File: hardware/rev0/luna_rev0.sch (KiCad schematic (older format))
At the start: 34 parts, among them J1 USB_B_Micro, J2 USB_B_Micro, J3 USB_A, J4 USB_B_Micro, J7 Conn_02x02_Counter_Clockwise, J8 Conn_Coaxial, J9 Conn_Coaxial, SW1 BTN_RECOVERY, SW2 BTN_DFU, SW3 BTN_RESET, U1 AP22814-SOT, U12 AP22814-SOT, Y1 DSC60xx

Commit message: hardware: add part numbers
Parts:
- C53: Description (none) -> CAP CER 10UF 10V X5R 0805; Manufacturer_Name (none) -> Taiyo Yuden; Manufacturer_Part_Number (none) -> LMK212ABJ106KGHT
- D1, D8: Description (none) -> DIODE SCHOTTKY 30V 5A SOD128; Manufacturer_Name (none) -> Nexperia; Manufacturer_Part_Number (none) -> PMEG3050EP,115
- D2: Manufacturer_Part_Number (none) -> GENERIC-LED-0603-RED
- D3: Manufacturer_Part_Number (none) -> GENERIC-LED-0603-ORANGE
- D4: Manufacturer_Part_Number (none) -> GENERIC-LED-0603-YELLOW
- D5: Manufacturer_Part_Number (none) -> GENERIC-LED-0603-GREEN
- D6: Manufacturer_Part_Number (none) -> GENERIC-LED-0603-BLUE
- D7: Manufacturer_Part_Number (none) -> GENERIC-LED-0603-PURPLE
- J1, J2, J4: Description (none) -> CONN RCPT USB2.0 MICRO B SMD R/A; Manufacturer_Name (none) -> Amphenol ICC; Manufacturer_Part_Number (none) -> 10103594-0001LF
- J3: Description (none) -> CONN RCPT USB2.0 TYPEA 4POS R/A; Manufacturer_Name (none) -> Amphenol ICC; Manufacturer_Part_Number (none) -> UE27AC54100
- R1, R2, R3: Manufacturer_Part_Number (none) -> GENERIC-RES-0402-10K
- R26, R27, R28, R29, R30, R31: Manufacturer_Part_Number (none) -> GENERIC-RES-0402-330
- SW1, SW2, SW3: Description (none) -> SWITCH TACTILE SPST-NO 0.05A 24V; Manufacturer_Name (none) -> TE Connectivity; Manufacturer_Part_Number (none) -> 1825027-5
- U1, U12: Description (none) -> IC PWR SWITCH P-CHAN 1:1 SOT25; Manufacturer_Name (none) -> Diodes Inc.; Manufacturer_Part_Number (none) -> AP22814AW5-7
- Y1: Description (none) -> MEMS OSC XO 60.0000MHZ CMOS SMD; Manufacturer_Name (none) -> Microchip; Manufacturer_Part_Number (none) -> DSC6001MI2A-060.0000
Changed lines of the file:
@@
 EESchema Schematic File Version 4
-LIBS:luna_rev0-cache
 EELAYER 30 0
 EELAYER END
@@
 F 2 "luna:SOD128" H 6300 4850 50  0001 C CNN
 F 3 "~" H 6300 4850 50  0001 C CNN
+F 4 "Nexperia" H 6300 4850 50  0001 C CNN "Manufacturer_Name"
+F 5 "PMEG3050EP,115" H 6300 4850 50  0001 C CNN "Manufacturer_Part_Number"
+F 6 "DIODE SCHOTTKY 30V 5A SOD128" H 6300 4850 50  0001 C CNN "Description"
 	1    6300 4850
 	1    0    0    -1
@@
 F 2 "Connector_USB:USB_Micro-B_Amphenol_10103594-0001LF_Horizontal" H 7250 5000 50  0001 C CNN
 F 3 "~" H 7250 5000 50  0001 C CNN
+F 4 "CONN RCPT USB2.0 MICRO B SMD R/A" H 7100 5050 50  0001 C CNN "Description"
+F 5 "Amphenol ICC" H 7100 5050 50  0001 C CNN "Manufacturer_Name"
+F 6 "10103594-0001LF" H 7100 5050 50  0001 C CNN "Manufacturer_Part_Number"
 	1    7100 5050
 	-1   0    0    -1
@@
 F 2 "Connector_USB:USB_Micro-B_Amphenol_10103594-0001LF_Horizontal" H 1050 3850 50  0001 C CNN
 F 3 "~" H 1050 3850 50  0001 C CNN
+F 4 "CONN RCPT USB2.0 MICRO B SMD R/A" H 900 3900 50  0001 C CNN "Description"
+F 5 "Amphenol ICC" H 900 3900 50  0001 C CNN "Manufacturer_Name"
+F 6 "10103594-0001LF" H 900 3900 50  0001 C CNN "Manufacturer_Part_Number"
 	1    900  3900
 	1    0    0    -1
@@
 F 2 "luna:SOD128" H 1500 3550 50  0001 C CNN
 F 3 "~" H 1500 3550 50  0001 C CNN
+F 4 "Nexperia" H 1500 3550 50  0001 C CNN "Manufacturer_Name"
+F 5 "PMEG3050EP,115" H 1500 3550 50  0001 C CNN "Manufacturer_Part_Number"
+F 6 "DIODE SCHOTTKY 30V 5A SOD128" H 1500 3550 50  0001 C CNN "Description"
 	1    1500 3550
 	-1   0    0    1
@@
 F 2 "luna:CONN-Amphenol-UE27AC54100" H 9100 2400 50  0001 C CNN
 F 3 " ~" H 9100 2400 50  0001 C CNN
+F 4 "CONN RCPT USB2.0 TYPEA 4POS R/A" H 8950 2450 50  0001 C CNN "Description"
+F 5 "Amphenol ICC" H 8950 2450 50  0001 C CNN "Manufacturer_Name"
+F 6 "UE27AC54100" H 8950 2450 50  0001 C CNN "Manufacturer_Part_Number"
 	1    8950 2450
 	-1   0    0    -1
@@
 F 2 "Connector_USB:USB_Micro-B_Amphenol_10103594-0001LF_Horizontal" H 9150 3700 50  0001 C CNN
 F 3 "~" H 9150 3700 50  0001 C CNN
+F 4 "CONN RCPT USB2.0 MICRO B SMD R/A" H 9000 3750 50  0001 C CNN "Description"
+F 5 "Amphenol ICC" H 9000 3750 50  0001 C CNN "Manufacturer_Name"
+F 6 "10103594-0001LF" H 9000 3750 50  0001 C CNN "Manufacturer_Part_Number"
 	1    9000 3750
 	-1   0    0    -1
@@
 F 2 "Resistor_SMD:R_0402_1005Metric" V 7880 1700 50  0001 C CNN
 F 3 "~" H 7950 1700 50  0001 C CNN
+F 4 "GENERIC-RES-0402-10K" H 7950 1700 50  0001 C CNN "Manufacturer_Part_Number"
 	1    7950 1700
 	0    1    -1   0
@@
 F 2 "Crystal:Crystal_SMD_2016-4Pin_2.0x1.6mm" H 1050 2400 50  0001 C CNN
 F 3 "" H 1050 2400 50  0001 C CNN
+F 4 "MEMS OSC XO 60.0000MHZ CMOS SMD" H 1050 2400 50  0001 C CNN "Description"
+F 5 "Microchip" H 1050 2400 50  0001 C CNN "Manufacturer_Name"
+F 6 "DSC6001MI2A-060.0000" H 1050 2400 50  0001 C CNN "Manufacturer_Part_Number"
 	1    1050 2400
 	1    0    0    -1
@@
 F 2 "luna:SWITCH-FSMRA" H 2250 5350 50  0001 C CNN
 F 3 "~" H 2250 5350 50  0001 C CNN
+F 4 "SWITCH TACTILE SPST-NO 0.05A 24V" H 2250 5350 50  0001 C CNN "Description"
+F 5 "TE Connectivity" H 2250 5350 50  0001 C CNN "Manufacturer_Name"
+F 6 "1825027-5" H 2250 5350 50  0001 C CNN "Manufacturer_Part_Number"
 	1    2250 5350
 	1    0    0    -1
@@
 F 2 "luna:SWITCH-FSMRA" H 2250 5650 50  0001 C CNN
 F 3 "~" H 2250 5650 50  0001 C CNN
+F 4 "SWITCH TACTILE SPST-NO 0.05A 24V" H 2250 5650 50  0001 C CNN "Description"
+F 5 "TE Connectivity" H 2250 5650 50  0001 C CNN "Manufacturer_Name"
+F 6 "1825027-5" H 2250 5650 50  0001 C CNN "Manufacturer_Part_Number"
 	1    2250 5650
 	1    0    0    -1
@@
 F 2 "luna:SWITCH-FSMRA" H 2250 6000 50  0001 C CNN
 F 3 "~" H 2250 6000 50  0001 C CNN
+F 4 "SWITCH TACTILE SPST-NO 0.05A 24V" H 2250 6000 50  0001 C CNN "Description"
+F 5 "TE Connectivity" H 2250 6000 50  0001 C CNN "Manufacturer_Name"
+F 6 "1825027-5" H 2250 6000 50  0001 C CNN "Manufacturer_Part_Number"
 	1    2250 6000
 	1    0    0    -1
@@
 F 2 "Resistor_SMD:R_0402_1005Metric" V 9380 4900 50  0001 C CNN
 F 3 "~" H 9450 4900 50  0001 C CNN
+F 4 "GENERIC-RES-0402-330" H 9450 4900 50  0001 C CNN "Manufacturer_Part_Number"
 	1    9450 4900
 	0    1    1    0
@@
 F 2 "Resistor_SMD:R_0402_1005Metric" V 9380 5000 50  0001 C CNN
 F 3 "~" H 9450 5000 50  0001 C CNN
+F 4 "GENERIC-RES-0402-330" H 9450 5000 50  0001 C CNN "Manufacturer_Part_Number"
 	1    9450 5000
 	0    1    1    0
@@
 F 2 "Resistor_SMD:R_0402_1005Metric" V 9380 5100 50  0001 C CNN
 F 3 "~" H 9450 5100 50  0001 C CNN
+F 4 "GENERIC-RES-0402-330" H 9450 5100 50  0001 C CNN "Manufacturer_Part_Number"
 	1    9450 5100
 	0    1    1    0
@@
 F 2 "Resistor_SMD:R_0402_1005Metric" V 9380 5200 50  0001 C CNN
 F 3 "~" H 9450 5200 50  0001 C CNN
+F 4 "GENERIC-RES-0402-330" H 9450 5200 50  0001 C CNN "Manufacturer_Part_Number"
 	1    9450 5200
 	0    1    1    0
@@
 F 2 "Resistor_SMD:R_0402_1005Metric" V 9380 5300 50  0001 C CNN
 F 3 "~" H 9450 5300 50  0001 C CNN
+F 4 "GENERIC-RES-0402-330" H 9450 5300 50  0001 C CNN "Manufacturer_Part_Number"
 	1    9450 5300
 	0    1    1    0
@@
 F 2 "Resistor_SMD:R_0402_1005Metric" V 9380 5400 50  0001 C CNN
 F 3 "~" H 9450 5400 50  0001 C CNN
+F 4 "GENERIC-RES-0402-330" H 9450 5400 50  0001 C CNN "Manufacturer_Part_Number"
 	1    9450 5400
 	0    1    1    0
@@
 F 2 "LED_SMD:LED_0603_1608Metric_Pad1.05x0.95mm_HandSolder" H 9950 4900 50  0001 C CNN
 F 3 "~" H 9950 4900 50  0001 C CNN
+F 4 "GENERIC-LED-0603-RED" H 9950 4900 50  0001 C CNN "Manufacturer_Part_Number"
 	1    9950 4900
 	1    0    0    -1
@@
 F 2 "LED_SMD:LED_0603_1608Metric_Pad1.05x0.95mm_HandSolder" H 9950 5100 50  0001 C CNN
 F 3 "~" H 9950 5100 50  0001 C CNN
+F 4 "GENERIC-LED-0603-YELLOW" H 9950 5100 50  0001 C CNN "Manufacturer_Part_Number"
 	1    9950 5100
 	1    0    0    -1
@@
 F 2 "LED_SMD:LED_0603_1608Metric_Pad1.05x0.95mm_HandSolder" H 9950 5200 50  0001 C CNN
 F 3 "~" H 9950 5200 50  0001 C CNN
+F 4 "GENERIC-LED-0603-GREEN" H 9950 5200 50  0001 C CNN "Manufacturer_Part_Number"
 	1    9950 5200
 	1    0    0    -1
@@
 F 2 "LED_SMD:LED_0603_1608Metric_Pad1.05x0.95mm_HandSolder" H 9950 5300 50  0001 C CNN
 F 3 "~" H 9950 5300 50  0001 C CNN
+F 4 "GENERIC-LED-0603-BLUE" H 9950 5300 50  0001 C CNN "Manufacturer_Part_Number"
 	1    9950 5300
 	1    0    0    -1
@@
 F 2 "LED_SMD:LED_0603_1608Metric_Pad1.05x0.95mm_HandSolder" H 9950 5400 50  0001 C CNN
 F 3 "~" H 9950 5400 50  0001 C CNN
+F 4 "GENERIC-LED-0603-PURPLE" H 9950 5400 50  0001 C CNN "Manufacturer_Part_Number"
 	1    9950 5400
 	1    0    0    -1
@@
 F 2 "gsg-modules:SOT25" H 8800 1450 50  0001 C CNN
 F 3 "" H 8800 1450 50  0001 C CNN
+F 4 "IC PWR SWITCH P-CHAN 1:1 SOT25" H 8800 1450 50  0001 C CNN "Description"
+F 5 "Diodes Inc." H 8800 1450 50  0001 C CNN "Manufacturer_Name"
+F 6 "AP22814AW5-7" H 8800 1450 50  0001 C CNN "Manufacturer_Part_Number"
 	1    8800 1450
 	1    0    0    -1
@@
 F 2 "Resistor_SMD:R_0402_1005Metric" V 7880 1050 50  0001 C CNN
 F 3 "~" H 7950 1050 50  0001 C CNN
+F 4 "GENERIC-RES-0402-10K" H 7950 1050 50  0001 C CNN "Manufacturer_Part_Number"
 	1    7950 1050
 	0    -1   1    0
@@
 F 2 "gsg-modules:SOT25" H 8800 800 50  0001 C CNN
 F 3 "" H 8800 800 50  0001 C CNN
+F 4 "IC PWR SWITCH P-CHAN 1:1 SOT25" H 8800 800 50  0001 C CNN "Description"
+F 5 "Diodes Inc." H 8800 800 50  0001 C CNN "Manufacturer_Name"
+F 6 "AP22814AW5-7" H 8800 800 50  0001 C CNN "Manufacturer_Part_Number"
 	1    8800 800
 	1    0    0    -1
@@
 F 2 "Capacitor_SMD:C_0402_1005Metric" V 6730 4050 50  0001 C CNN
 F 3 "~" H 6800 4050 50  0001 C CNN
+F 4 "GENERIC-RES-0402-10K" H 6800 4050 50  0001 C CNN "Manufacturer_Part_Number"
 	1    6800 4050
 	0    1    1    0
@@
 F 2 "Capacitor_SMD:C_0805_2012Metric" H 10888 800 50  0001 C CNN
 F 3 "~" H 10850 950 50  0001 C CNN
+F 4 "CAP CER 10UF 10V X5R 0805" H 10850 950 50  0001 C CNN "Description"
+F 5 "Taiyo Yuden" H 10850 950 50  0001 C CNN "Manufacturer_Name"
+F 6 "LMK212ABJ106KGHT" H 10850 950 50  0001 C CNN "Manufacturer_Part_Number"
 	1    10850 950
 	0    1    1    0
@@
 F 2 "LED_SMD:LED_0603_1608Metric_Pad1.05x0.95mm_HandSolder" H 9950 5000 50  0001 C CNN
 F 3 "~" H 9950 5000 50  0001 C CNN
+F 4 "GENERIC-LED-0603-ORANGE" H 9950 5000 50  0001 C CNN "Manufacturer_Part_Number"
 	1    9950 5000
 	1    0    0    -1

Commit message: hardware: correct R3 footprint
fix #11
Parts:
- R3: footprint Capacitor_SMD:C_0402_1005Metric -> Resistor_SMD:R_0402_1005Metric
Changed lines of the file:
@@
 F 0 "R3" V 6900 4050 50  0000 C CNN
 F 1 "10K" V 6800 4050 50  0000 C CNN
-F 2 "Capacitor_SMD:C_0402_1005Metric" V 6730 4050 50  0001 C CNN
+F 2 "Resistor_SMD:R_0402_1005Metric" V 6730 4050 50  0001 C CNN
 F 3 "~" H 6800 4050 50  0001 C CNN
 F 4 "GENERIC-RES-0402-10K" H 6800 4050 50  0001 C CNN "Manufacturer_Part_Number"

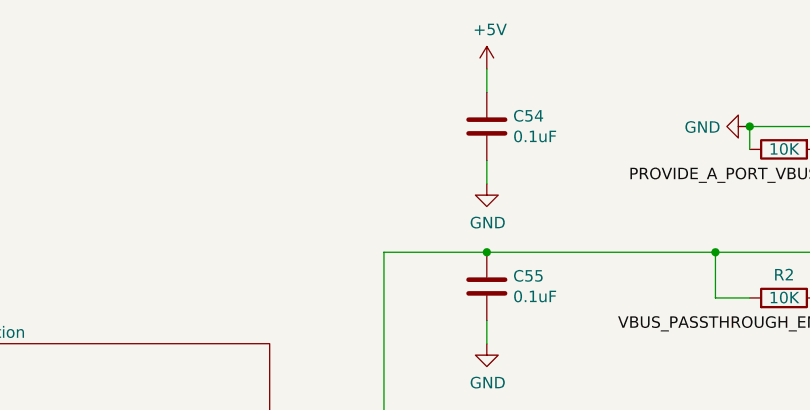
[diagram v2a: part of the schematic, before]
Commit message: hardware: update capacitors in schematic
Add parts that were in layout but were missing from schematic.
Update schematic to better represent r0.2 as manufactured.
fix #10
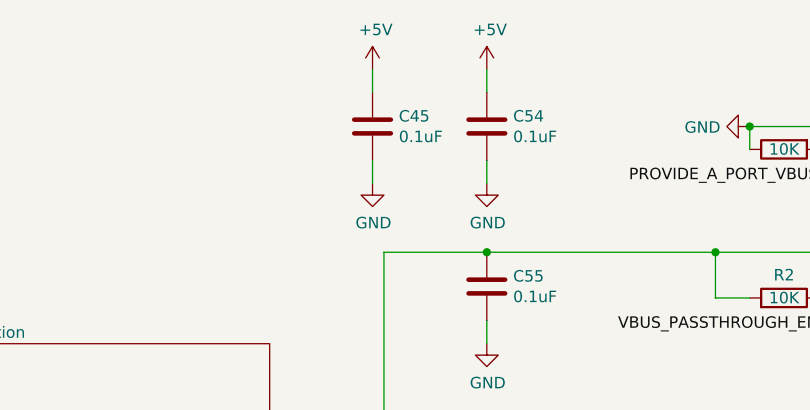
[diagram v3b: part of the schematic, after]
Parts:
- added C45: 0.1uF, Capacitor_SMD:C_0402_1005Metric, symbol Device:C
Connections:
- net +5V: now also C45.1
- net GND: now also C45.2
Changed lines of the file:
@@
 Wire Wire Line
 	5850 6050 5700 6050
+$Comp
+L Device:C C45
+U 1 1 5EE7CC33
+P 6150 950
+F 0 "C45" H 6265 995 50  0000 L CNN
+F 1 "0.1uF" H 6265 905 50  0000 L CNN
+F 2 "Capacitor_SMD:C_0402_1005Metric" H 6188 800 50  0001 C CNN
+F 3 "~" H 6150 950 50  0001 C CNN
+	1    6150 950
+	1    0    0    -1
+$EndComp
+$Comp
+L power:GND #PWR0122
+U 1 1 5EE7CC3D
+P 6150 1200
+F 0 "#PWR0122" H 6150 950 50  0001 C CNN
+F 1 "GND" H 6154 1028 50  0000 C CNN
+F 2 "" H 6150 1200 50  0001 C CNN
+F 3 "" H 6150 1200 50  0001 C CNN
+	1    6150 1200
+	1    0    0    -1
+$EndComp
+Wire Wire Line
+	6150 1200 6150 1100
+$Comp
+L power:+5V #PWR0123
+U 1 1 5EE7CC48
+P 6150 700
+F 0 "#PWR0123" H 6150 550 50  0001 C CNN
+F 1 "+5V" H 6164 873 50  0000 C CNN
+F 2 "" H 6150 700 50  0001 C CNN
+F 3 "" H 6150 700 50  0001 C CNN
+	1    6150 700
+	1    0    0    -1
+$EndComp
+Wire Wire Line
+	6150 700  6150 800
 $EndSCHEMATC

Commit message: hardware: normalize BOM fields
make compatible with kicad-bom-scripts
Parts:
- C45, C54, C55: Part Number (none) -> GENERIC-CAP-0402-0.1uF
- C53: Manufacturer (none) -> Taiyo Yuden; Manufacturer_Name Taiyo Yuden -> (none); Manufacturer_Part_Number LMK212ABJ106KGHT -> (none); Part Number (none) -> LMK212ABJ106KGHT
- D1, D8: Manufacturer (none) -> Nexperia; Manufacturer_Name Nexperia -> (none); Manufacturer_Part_Number PMEG3050EP,115 -> (none); Part Number (none) -> PMEG3050EP,115
- D2: Manufacturer_Part_Number GENERIC-LED-0603-RED -> (none); Part Number (none) -> GENERIC-LED-0603-RED
- D3: Manufacturer_Part_Number GENERIC-LED-0603-ORANGE -> (none); Part Number (none) -> GENERIC-LED-0603-ORANGE
- D4: Manufacturer_Part_Number GENERIC-LED-0603-YELLOW -> (none); Part Number (none) -> GENERIC-LED-0603-YELLOW
- D5: Manufacturer_Part_Number GENERIC-LED-0603-GREEN -> (none); Part Number (none) -> GENERIC-LED-0603-GREEN
- D6: Manufacturer_Part_Number GENERIC-LED-0603-BLUE -> (none); Part Number (none) -> GENERIC-LED-0603-BLUE
- D7: Manufacturer_Part_Number GENERIC-LED-0603-PURPLE -> (none); Part Number (none) -> GENERIC-LED-0603-PURPLE
- J1, J2, J4: Manufacturer (none) -> Amphenol ICC; Manufacturer_Name Amphenol ICC -> (none); Manufacturer_Part_Number 10103594-0001LF -> (none); Part Number (none) -> 10103594-0001LF
- J3: Manufacturer (none) -> Amphenol ICC; Manufacturer_Name Amphenol ICC -> (none); Manufacturer_Part_Number UE27AC54100 -> (none); Part Number (none) -> UE27AC54100
- R1, R2, R3: Manufacturer_Part_Number GENERIC-RES-0402-10K -> (none); Part Number (none) -> GENERIC-RES-0402-10K
- R26, R27, R28, R29, R30, R31: Manufacturer_Part_Number GENERIC-RES-0402-330 -> (none); Part Number (none) -> GENERIC-RES-0402-330
- SW1, SW2, SW3: Manufacturer (none) -> TE Connectivity; Manufacturer_Name TE Connectivity -> (none); Manufacturer_Part_Number 1825027-5 -> (none); Part Number (none) -> 1825027-5
- U1, U12: Manufacturer (none) -> Diodes Inc.; Manufacturer_Name Diodes Inc. -> (none); Manufacturer_Part_Number AP22814AW5-7 -> (none); Part Number (none) -> AP22814AW5-7
- Y1: Manufacturer (none) -> Microchip; Manufacturer_Name Microchip -> (none); Manufacturer_Part_Number DSC6001MI2A-060.0000 -> (none); Part Number (none) -> DSC6001MI2A-060.0000
